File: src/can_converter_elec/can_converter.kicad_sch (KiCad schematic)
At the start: 10 parts, among them J1 SM02B-PASS, X1 629722000214_pasteInHole

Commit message: Cleanup can conv (#77)
* Remove v1 can converter (Candlelight), canonicalize v2, update readme

* Move can_conv_v2 -> can_conv

* Add basic documentation

* Remove files that were previously tracked unintentionally

* Oops, Move can_conv -> can_conv_elec, ditto for can_term, swd_adapter

* Fix symbol and footprint tables

* Remove generated netlist

* Move monke out of bluesat footprints, add more metadata to bluesat syms

* Add TypeC connector to bluesat syms/fp

---------

Co-authored-by: Cyreqs <seanhaines2007@gmail.com>
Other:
- sheet CAN Transceiver ports: added none; removed CAN2_H, CAN2_L, CAN2_RX, CAN2_S, CAN2_TX
- sheet MCU ports: added none; removed CAN2_RX, CAN2_S, CAN2_TX
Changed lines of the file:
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@@
+	)
+	(junction
+		(at 15.24 64.77)
+		(diameter 0)
+		(color 0 0 0 0)
 	)
 	(junction
@@
 	)
 	(junction
+		(at 15.24 78.74)
+		(diameter 0)
+		(color 0 0 0 0)
+	)
+	(junction
 		(at 15.24 62.23)
 		(diameter 0)
@@
 	(wire
 		(pts
-			(xy 113.03 83.82) (xy 115.57 83.82)
-		)
-		(stroke
-			(width 0)
-			(type default)
-		)
-	)
-	(wire
-		(pts
 			(xy 229.87 132.08) (xy 229.87 142.24)
 		)
@@
 	(wire
 		(pts
-			(xy 113.03 81.28) (xy 115.57 81.28)
-		)
-		(stroke
-			(width 0)
-			(type default)
-		)
-	)
-	(wire
-		(pts
 			(xy 252.73 114.3) (xy 252.73 115.57)
 		)
@@
 	(wire
 		(pts
-			(xy 142.24 78.74) (xy 151.13 78.74)
-		)
-		(stroke
-			(width 0)
-			(type default)
-		)
-	)
-	(wire
-		(pts
 			(xy 15.24 81.28) (xy 21.59 81.28)
 		)
@@
 		(pts
 			(xy 48.26 64.77) (xy 78.74 64.77)
-		)
-		(stroke
-			(width 0)
-			(type default)
-		)
-	)
-	(wire
-		(pts
-			(xy 142.24 81.28) (xy 151.13 81.28)
-		)
-		(stroke
-			(width 0)
-			(type default)
-		)
-	)
-	(wire
-		(pts
-			(xy 113.03 78.74) (xy 115.57 78.74)
 		)
 		(stroke
@@
 		)
 	)
-	(label "CAN2_L"
-		(at 151.13 81.28 180)
-		(effects
-			(font
-				(size 1.27 1.27)
-			)
-			(justify right bottom)
-		)
-	)
 	(label "USB_N"
 		(at 55.88 67.31 180)
@@
 		)
 	)
-	(label "CAN2_H"
-		(at 151.13 78.74 180)
-		(effects
-			(font
-				(size 1.27 1.27)
-			)
-			(justify right bottom)
+	(symbol
+		(lib_id "power:PWR_FLAG")
+		(at 15.24 78.74 0)
+		(unit 1)
+		(exclude_from_sim no)
+		(in_bom yes)
+		(on_board yes)
+		(dnp no)
+		(fields_autoplaced yes)
+		(property "Reference" "#FLG01"
+			(at 15.24 76.835 0)
+			(effects
+				(font
+					(size 1.27 1.27)
+				)
+				(hide yes)
+			)
+		)
+		(property "Value" "PWR_FLAG"
+			(at 15.24 73.66 0)
+			(effects
+				(font
+					(size 1.27 1.27)
+				)
+				(hide yes)
+			)
+		)
+		(property "Footprint" ""
+			(at 15.24 78.74 0)
+			(effects
+				(font
+					(size 1.27 1.27)
+				)
+				(hide yes)
+			)
+		)
+		(property "Datasheet" "~"
+			(at 15.24 78.74 0)
+			(effects
+				(font
+					(size 1.27 1.27)
+				)
+				(hide yes)
+			)
+		)
+		(property "Description" "Special symbol for telling ERC where power comes from"
+			(at 15.24 78.74 0)
+			(effects
+				(font
+					(size 1.27 1.27)
+				)
+				(hide yes)
+			)
+		)
+		(pin "1"
+		)
+		(instances
+			(project ""
+				(path "/e63e39d7-6ac0-4ffd-8aa3-1841a4541b55"
+					(reference "#FLG01")
+					(unit 1)
+				)
+			)
 		)
 	)
@@
 	)
 	(symbol
+		(lib_id "power:PWR_FLAG")
+		(at 15.24 64.77 180)
+		(unit 1)
+		(exclude_from_sim no)
+		(in_bom yes)
+		(on_board yes)
+		(dnp no)
+		(fields_autoplaced yes)
+		(property "Reference" "#FLG03"
+			(at 15.24 66.675 0)
+			(effects
+				(font
+					(size 1.27 1.27)
+				)
+				(hide yes)
+			)
+		)
+		(property "Value" "PWR_FLAG"
+			(at 15.24 69.85 0)
+			(effects
+				(font
+					(size 1.27 1.27)
+				)
+				(hide yes)
+			)
+		)
+		(property "Footprint" ""
+			(at 15.24 64.77 0)
+			(effects
+				(font
+					(size 1.27 1.27)
+				)
+				(hide yes)
+			)
+		)
+		(property "Datasheet" "~"
+			(at 15.24 64.77 0)
+			(effects
+				(font
+					(size 1.27 1.27)
+				)
+				(hide yes)
+			)
+		)
+		(property "Description" "Special symbol for telling ERC where power comes from"
+			(at 15.24 64.77 0)
+			(effects
+				(font
+					(size 1.27 1.27)
+				)
+				(hide yes)
+			)
+		)
+		(pin "1"
+		)
+		(instances
+			(project ""
+				(path "/e63e39d7-6ac0-4ffd-8aa3-1841a4541b55"
+					(reference "#FLG03")
+					(unit 1)
+				)
+			)
+		)
+	)
+	(symbol
 		(lib_id "Res_1Percent_E24_0603_100mW_-40C-90C:1k_0603_100mW_1%_E24_Chip-Resistor")
 		(at 229.87 119.38 0)
@@
 		)
 		(instances
-			(project "Can_converter_v2"
+			(project "can_converter"
 				(path "/e63e39d7-6ac0-4ffd-8aa3-1841a4541b55"
 					(page "3")
@@
 			)
 		)
-		(pin "CAN2_H" bidirectional
-			(at 142.24 78.74 0)
-			(effects
-				(font
-					(size 1.27 1.27)
-				)
-				(justify right)
-			)
-		)
-		(pin "CAN2_L" bidirectional
-			(at 142.24 81.28 0)
-			(effects
-				(font
-					(size 1.27 1.27)
-				)
-				(justify right)
-			)
-		)
-		(pin "CAN2_TX" input
-			(at 115.57 78.74 180)
-			(effects
-				(font
-					(size 1.27 1.27)
-				)
-				(justify left)
-			)
-		)
-		(pin "CAN2_RX" output
-			(at 115.57 81.28 180)
-			(effects
-				(font
-					(size 1.27 1.27)
-				)
-				(justify left)
-			)
-		)
-		(pin "CAN2_S" input
-			(at 115.57 83.82 180)
-			(effects
-				(font
-					(size 1.27 1.27)
-				)
-				(justify left)
-			)
-		)
 		(pin "CAN1_RX" output
 			(at 115.57 67.31 180)
@@
 		)
 		(instances
-			(project "Can_converter_v2"
+			(project "can_converter"
 				(path "/e63e39d7-6ac0-4ffd-8aa3-1841a4541b55"
 					(page "4")
@@
 			)
 		)
-		(pin "CAN2_RX" input
-			(at 113.03 81.28 0)
-			(effects
-				(font
-					(size 1.27 1.27)
-				)
-				(justify right)
-			)
-		)
-		(pin "CAN2_TX" output
-			(at 113.03 78.74 0)
-			(effects
-				(font
-					(size 1.27 1.27)
-				)
-				(justify right)
-			)
-		)
 		(pin "CAN1_TX" output
 			(at 113.03 64.77 0)
@@
 			)
 		)
-		(pin "CAN2_S" output
-			(at 113.03 83.82 0)
-			(effects
-				(font
-					(size 1.27 1.27)
-				)
-				(justify right)
-			)
-		)
 		(pin "LED_RX" output
 			(at 113.03 95.25 0)
@@
 		)
 		(instances
-			(project "Can_converter_v2"
+			(project "can_converter"
 				(path "/e63e39d7-6ac0-4ffd-8aa3-1841a4541b55"
 					(page "2")

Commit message: remove mystery pull down resistor
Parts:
- X1: footprint Bluesat:USB_C -> Bluesat:USB_C_Receptacle_USB2.0_14P
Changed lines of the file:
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@@
 			)
 		)
-		(property "Footprint" "Bluesat:USB_C"
+		(property "Footprint" "Bluesat:USB_C_Receptacle_USB2.0_14P"
 			(at 33.02 55.88 0)
 			(effects

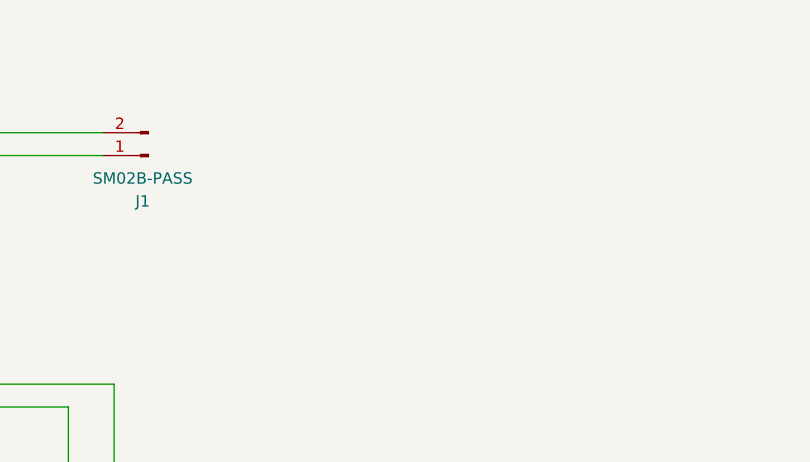
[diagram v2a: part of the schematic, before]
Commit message: Give in to Evan tism (remove IDC connector and add 2xM2.5 mounting holes)
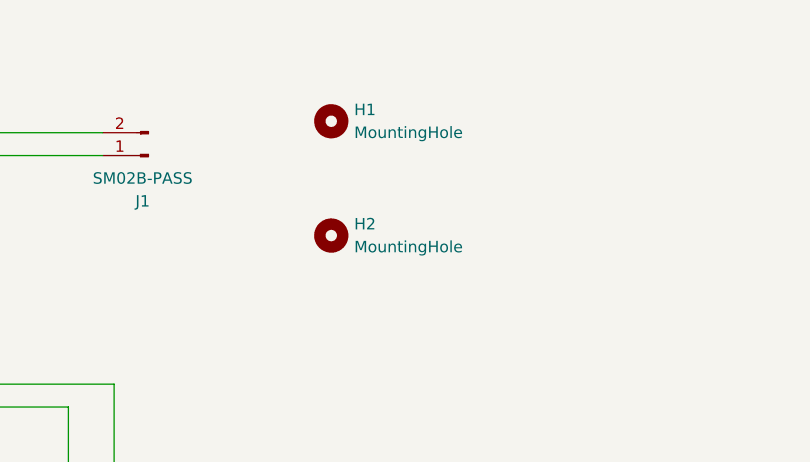
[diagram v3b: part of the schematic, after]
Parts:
- added H1, H2: MountingHole, Bluesat:M2.5, symbol Mechanical:MountingHole
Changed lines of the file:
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@@
+	)
+	(symbol
+		(lib_id "Mechanical:MountingHole")
+		(at 190.5 63.5 0)
+		(unit 1)
+		(exclude_from_sim no)
+		(in_bom no)
+		(on_board yes)
+		(dnp no)
+		(fields_autoplaced yes)
+		(property "Reference" "H1"
+			(at 193.04 62.2299 0)
+			(effects
+				(font
+					(size 1.27 1.27)
+				)
+				(justify left)
+			)
+		)
+		(property "Value" "MountingHole"
+			(at 193.04 64.7699 0)
+			(effects
+				(font
+					(size 1.27 1.27)
+				)
+				(justify left)
+			)
+		)
+		(property "Footprint" "Bluesat:M2.5"
+			(at 190.5 63.5 0)
+			(effects
+				(font
+					(size 1.27 1.27)
+				)
+				(hide yes)
+			)
+		)
+		(property "Datasheet" "~"
+			(at 190.5 63.5 0)
+			(effects
+				(font
+					(size 1.27 1.27)
+				)
+				(hide yes)
+			)
+		)
+		(property "Description" "Mounting Hole without connection"
+			(at 190.5 63.5 0)
+			(effects
+				(font
+					(size 1.27 1.27)
+				)
+				(hide yes)
+			)
+		)
+		(instances
+			(project ""
+				(path "/e63e39d7-6ac0-4ffd-8aa3-1841a4541b55"
+					(reference "H1")
+					(unit 1)
+				)
+			)
+		)
 	)
 	(symbol
@@
 					(unit 1)
 				)
+			)
+		)
+	)
+	(symbol
+		(lib_id "Mechanical:MountingHole")
+		(at 190.5 76.2 0)
+		(unit 1)
+		(exclude_from_sim no)
+		(in_bom no)
+		(on_board yes)
+		(dnp no)
+		(fields_autoplaced yes)
+		(property "Reference" "H2"
+			(at 193.04 74.9299 0)
+			(effects
+				(font
+					(size 1.27 1.27)
+				)
+				(justify left)
+			)
+		)
+		(property "Value" "MountingHole"
+			(at 193.04 77.4699 0)
+			(effects
+				(font
+					(size 1.27 1.27)
+				)
+				(justify left)
+			)
+		)
+		(property "Footprint" "Bluesat:M2.5"
+			(at 190.5 76.2 0)
+			(effects
+				(font
+					(size 1.27 1.27)
+				)
+				(hide yes)
+			)
+		)
+		(property "Datasheet" "~"
+			(at 190.5 76.2 0)
+			(effects
+				(font
+					(size 1.27 1.27)
+				)
+				(hide yes)
+			)
+		)
+		(property "Description" "Mounting Hole without connection"
+			(at 190.5 76.2 0)
+			(effects
+				(font
+					(size 1.27 1.27)
+				)
+				(hide yes)
+			)
+		)
+		(instances
+			(project "can_converter"
+				(path "/e63e39d7-6ac0-4ffd-8aa3-1841a4541b55"
+					(reference "H2")
+					(unit 1)
+				)
